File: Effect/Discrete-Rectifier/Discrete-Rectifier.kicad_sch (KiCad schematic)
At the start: 28 parts, among them J1 USB_C_Receptacle_USB2.0_16P, Q1 DMMT5551, Q2 DMMT5551

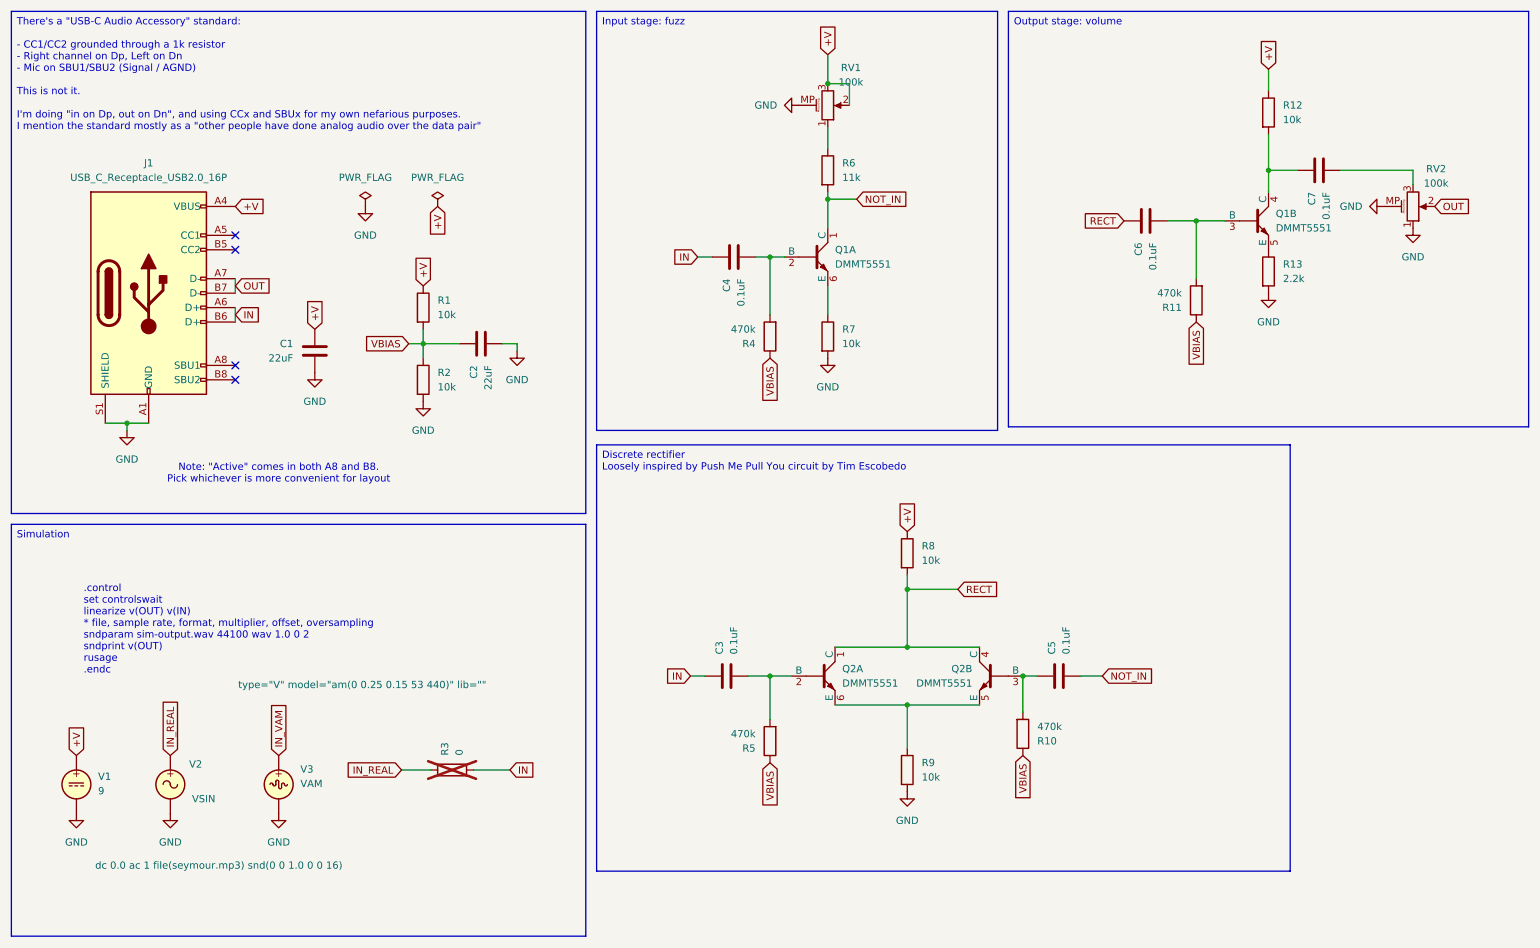
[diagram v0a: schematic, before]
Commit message: Convert the discrete test-boards to the new world order
The USB-C thing was good for testing things out, but not really
practical in real life.  So this just converts things to use the simpler
pin connector layout and the normal 1590A pot setup.

Both boards get a "brightness" pot, not because I think it makes much
sense, but because I standardized on the three-pot enclosure.

Signed-off-by: Linus Torvalds <torvalds@linux-foundation.org>
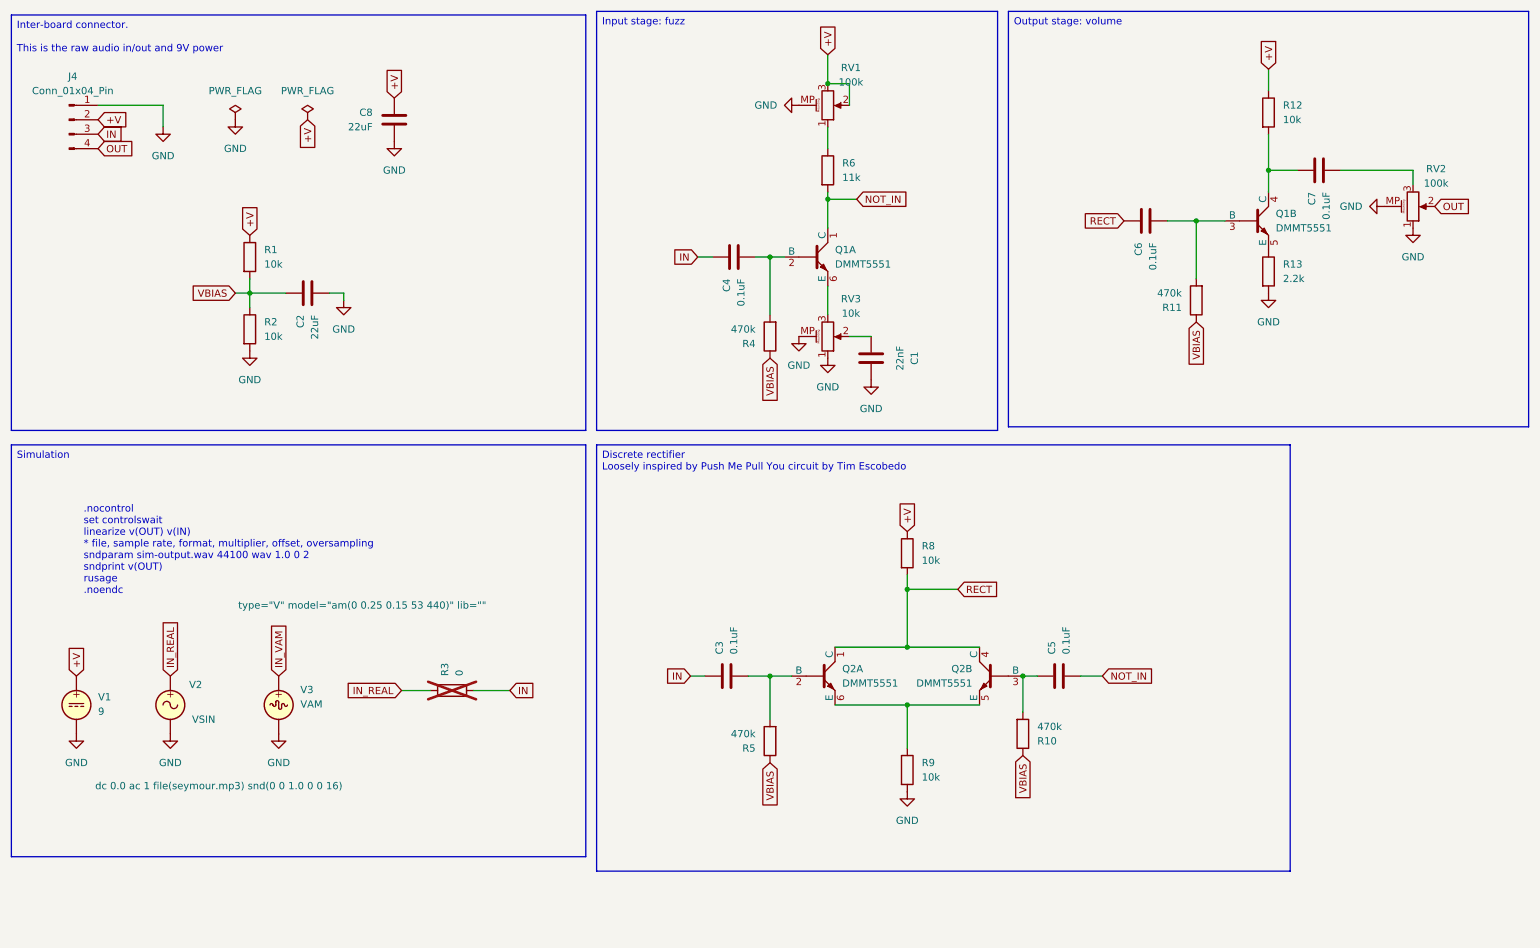
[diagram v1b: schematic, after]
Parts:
- removed J1: USB_C_Receptacle_USB2.0_16P, Connector_USB:USB_C_Receptacle_GCT_USB4085, symbol Connector:USB_C_Receptacle_USB2.0_16P
- removed R7: 10k, Resistor_SMD:R_0805_2012Metric, symbol Device:R
- added C8: 22uF, Capacitor_SMD:C_1206_3216Metric, symbol Device:C
- added J4: Conn_01x04_Pin, Connector_PinHeader_2.54mm:PinHeader_1x04_P2.54mm_Vertical, symbol Connector:Conn_01x04_Pin
- added RV3: 10k, Mylib:Potentiometer_9mm_MP, symbol Device:R_Potentiometer_MountingPin
- C1: value 22uF -> 22nF; footprint Capacitor_SMD:C_1206_3216Metric -> Capacitor_SMD:C_0805_2012Metric
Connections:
- net +V: now also C8.1, J4.2 (Pin_2); no longer C1.1
- net GND: now also C1.1, C8.2, J4.1 (Pin_1), RV3.1, RV3.MP (MountPin); no longer C1.2
- net IN: now also J4.3 (Pin_3)
- net OUT: now also J4.4 (Pin_4)
- net at Q1.6 (E): now also RV3.3
- new net: C1.2, RV3.2
- no-connect marks 4 -> 0
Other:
- note added: ".nocontrol set controlswait linearize v(OUT) v(IN) * file, sample rate, format, multiplier, offset, oversampling sndparam sim-output.wav 44100 wav 1.0 0 2 sndprint v(OUT) rusage .noendc"
- note removed: ".control set controlswait linearize v(OUT) v(IN) * file, sample rate, format, multiplier, offset, oversampling sndparam sim-output.wav 44100 wav 1.0 0 2 sndprint v(OUT) rusage .endc"
- note removed: "Note: "Active" comes in both A8 and B8. Pick whichever is more convenient for layout"
- moved on the sheet: C2, R1, R2, R3, V1, V2, V3
